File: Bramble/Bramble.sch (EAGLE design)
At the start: 29 parts

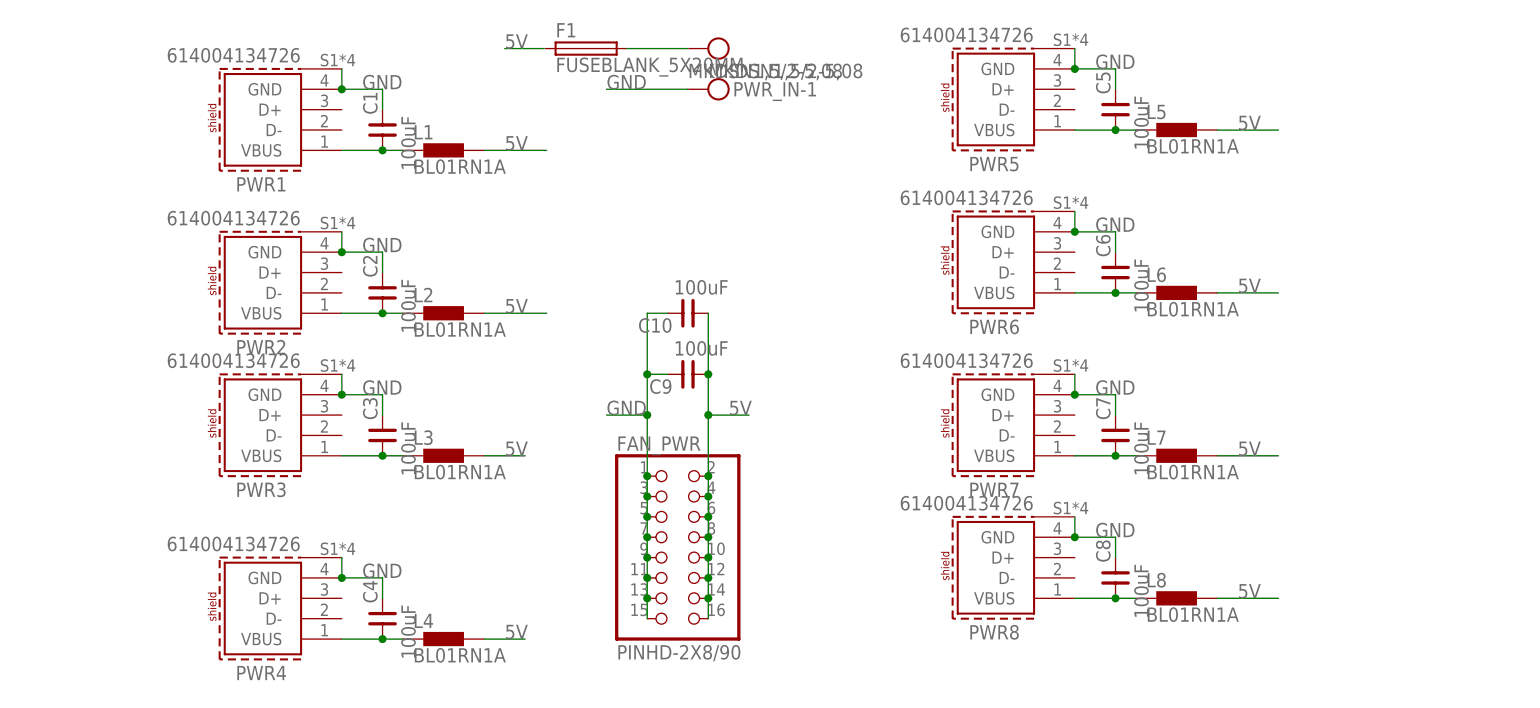
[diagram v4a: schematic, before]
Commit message: Reduction to 4 ports and SMD parts
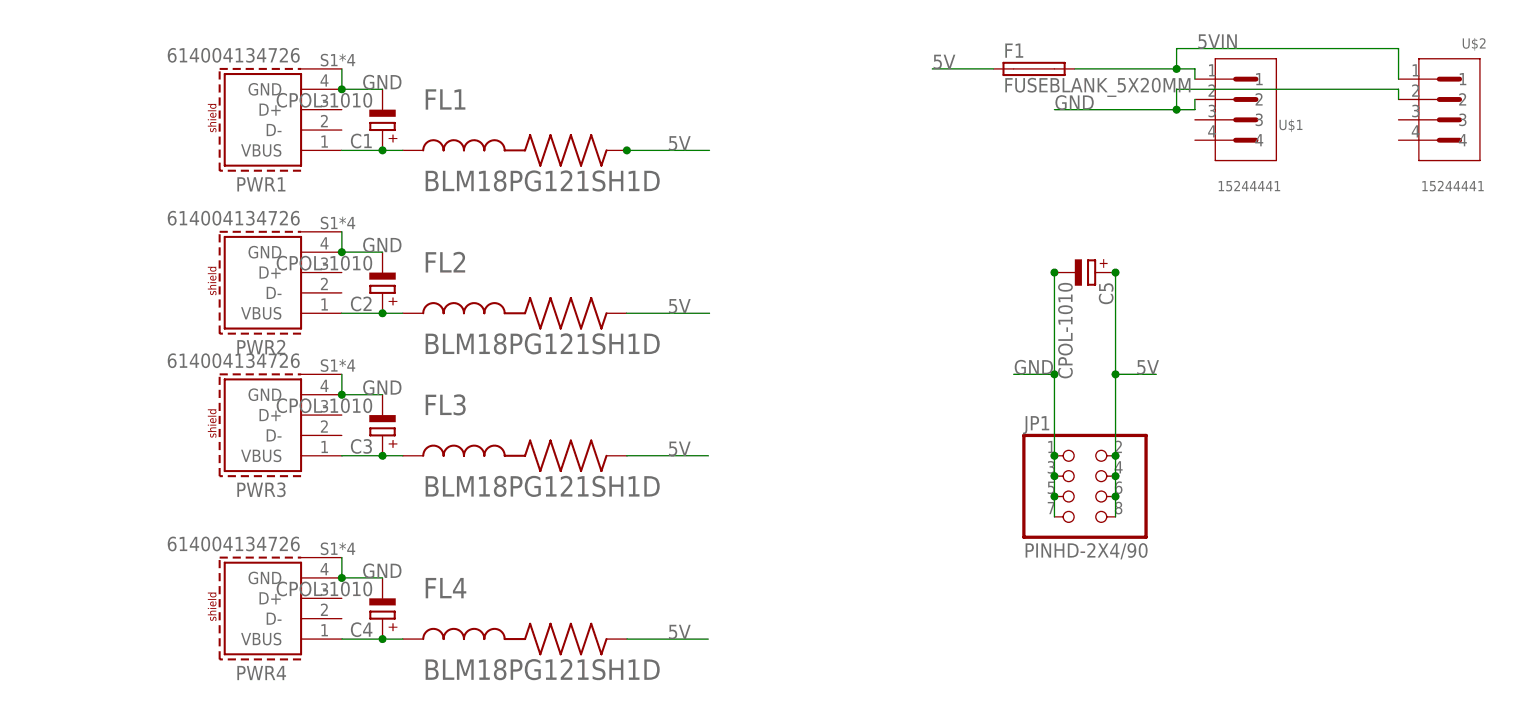
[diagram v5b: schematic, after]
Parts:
- removed C10, C6, C7, C8, C9: 100uF, cap-master:CBP-ENP-020-050
- removed FAN_PWR: PINHD-2X8/90, Connector:PINHD-2X8/90
- removed L1, L2, L3, L4, L5, L6, L7, L8: BL01RN1A, inductors:BL01RN1A
- removed PWR5, PWR6, PWR7, PWR8: 614004134726, Wurth_Connectors_WR-USB:614004134726
- removed PWR_IN: MKDSN1,5/2-5,08, con-phoenix-508:MKDSN1,5/2-5,08
- added FL1, FL2, FL3, FL4: BLM18PG121SH1D, BLM18PG121SH1D:BLM18PG121SH1D
- added JP1: PINHD-2X4/90, Connector:PINHD-2X4/90
- added U$1, U$2: 15244441, 15244441:15244441
- C1, C2, C3, C4, C5: value 100uF -> CPOL-1010; device cap-master:CBP-ENP-020-050 -> cap-vishay-153clv:CPOL-1010
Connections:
- removed net N$5: C5.1, L5.1, PWR5.VBUS
- removed net N$6: C6.1, L6.1, PWR6.VBUS
- removed net N$7: C7.1, L7.1, PWR7.VBUS
- removed net N$8: C8.1, L8.1, PWR8.VBUS
- removed net N$9: F1.2, PWR_IN-2.KL
- new net 5VIN: F1.2, U$1.1, U$2.1
- net 5V: now also C5.+, F1.1, FL1.2, FL2.2, FL3.2, FL4.2, JP1.2, JP1.4, JP1.6, JP1.8; no longer C10.1, C9.1, FAN_PWR.10, FAN_PWR.12, FAN_PWR.14, FAN_PWR.16, FAN_PWR.2, FAN_PWR.4, FAN_PWR.6, FAN_PWR.8, L1.2, L2.2, L3.2, L4.2, L5.2, L6.2, L7.2, L8.2
- net GND: now also C1.-, C2.-, C3.-, C4.-, C5.-, JP1.1, JP1.3, JP1.5, JP1.7, U$1.2, U$2.2; no longer C1.2, C10.2, C2.2, C3.2, C4.2, C5.2, C6.2, C7.2, C8.2, C9.2, FAN_PWR.1, FAN_PWR.11, FAN_PWR.13, FAN_PWR.15, FAN_PWR.3, FAN_PWR.5, FAN_PWR.7, FAN_PWR.9, PWR5.GND, PWR5.SHIELD, PWR6.GND, PWR6.SHIELD, PWR7.GND, PWR7.SHIELD, PWR8.GND, PWR8.SHIELD, PWR_IN-1.KL
- net N$1: now also C1.+, FL1.1; no longer C1.1, L1.1
- net N$2: now also C2.+, FL2.1; no longer C2.1, L2.1
- net N$3: now also C4.+, FL4.1; no longer C4.1, L4.1
- net N$4: now also C3.+, FL3.1; no longer C3.1, L3.1
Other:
- moved on the sheet: F1

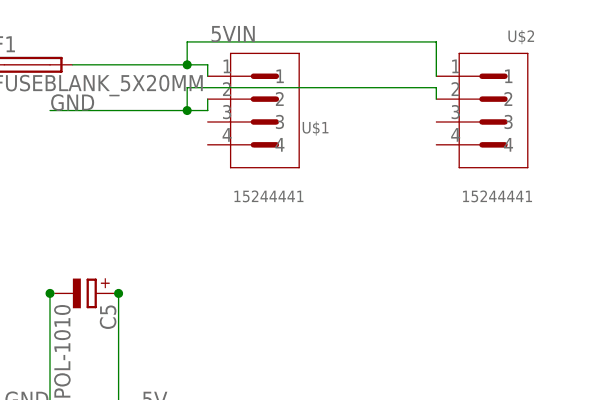
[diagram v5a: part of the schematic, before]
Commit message: Tweaked labels
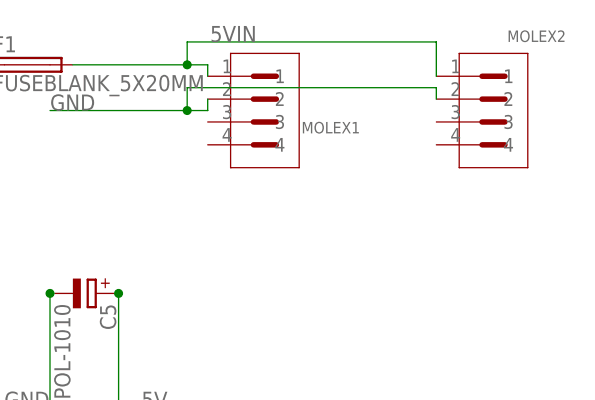
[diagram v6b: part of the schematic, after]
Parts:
- renumbered U$1 to MOLEX1, U$2 to MOLEX2
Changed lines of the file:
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@@
 <part name="FL3" library="BLM18PG121SH1D" deviceset="BLM18PG121SH1D" device=""/>
 <part name="FL4" library="BLM18PG121SH1D" deviceset="BLM18PG121SH1D" device=""/>
-<part name="U$1" library="15244441" deviceset="15244441" device=""/>
-<part name="U$2" library="15244441" deviceset="15244441" device=""/>
+<part name="MOLEX1" library="15244441" deviceset="15244441" device=""/>
+<part name="MOLEX2" library="15244441" deviceset="15244441" device=""/>
 </parts>
 <sheets>
@@
 <attribute name="VALUE" x="12.69" y="-2.546640625" size="2.54331875" layer="96"/>
 </instance>
-<instance part="U$1" gate="G$1" x="116.84" y="68.58" smashed="yes">
+<instance part="MOLEX1" gate="G$1" x="116.84" y="68.58" smashed="yes">
 <attribute name="NAME" x="119.37916875" y="66.041240625" size="1.270209375" layer="95"/>
-<attribute name="VALUE" x="111.75308125" y="58.4062" size="1.27173125" layer="96"/>
-</instance>
-<instance part="U$2" gate="G$1" x="142.24" y="68.58" smashed="yes">
+</instance>
+<instance part="MOLEX2" gate="G$1" x="142.24" y="68.58" smashed="yes">
 <attribute name="NAME" x="142.23916875" y="76.201240625" size="1.270209375" layer="95"/>
-<attribute name="VALUE" x="137.15308125" y="58.4062" size="1.27173125" layer="96"/>
 </instance>
 </instances>
@@
 <label x="91.44" y="68.58" size="1.778" layer="95"/>
 <wire x1="91.44" y1="68.58" x2="106.68" y2="68.58" width="0.1524" layer="91"/>
-<pinref part="U$1" gate="G$1" pin="2"/>
+<pinref part="MOLEX1" gate="G$1" pin="2"/>
 <wire x1="106.68" y1="68.58" x2="108.966" y2="68.58" width="0.1524" layer="91"/>
 <wire x1="108.966" y1="69.85" x2="108.966" y2="68.58" width="0.1524" layer="91"/>
-<pinref part="U$2" gate="G$1" pin="2"/>
+<pinref part="MOLEX2" gate="G$1" pin="2"/>
 <wire x1="134.366" y1="69.85" x2="134.366" y2="71.12" width="0.1524" layer="91"/>
 <wire x1="134.366" y1="71.12" x2="106.68" y2="71.12" width="0.1524" layer="91"/>
@@
 <pinref part="F1" gate="G$1" pin="2"/>
 <wire x1="93.98" y1="73.66" x2="106.68" y2="73.66" width="0.1524" layer="91"/>
-<pinref part="U$1" gate="G$1" pin="1"/>
+<pinref part="MOLEX1" gate="G$1" pin="1"/>
 <wire x1="106.68" y1="73.66" x2="108.966" y2="73.66" width="0.1524" layer="91"/>
 <wire x1="108.966" y1="72.39" x2="108.966" y2="73.66" width="0.1524" layer="91"/>
-<pinref part="U$2" gate="G$1" pin="1"/>
+<pinref part="MOLEX2" gate="G$1" pin="1"/>
 <wire x1="134.366" y1="72.39" x2="134.366" y2="76.2" width="0.1524" layer="91"/>
 <wire x1="134.366" y1="76.2" x2="106.68" y2="76.2" width="0.1524" layer="91"/>

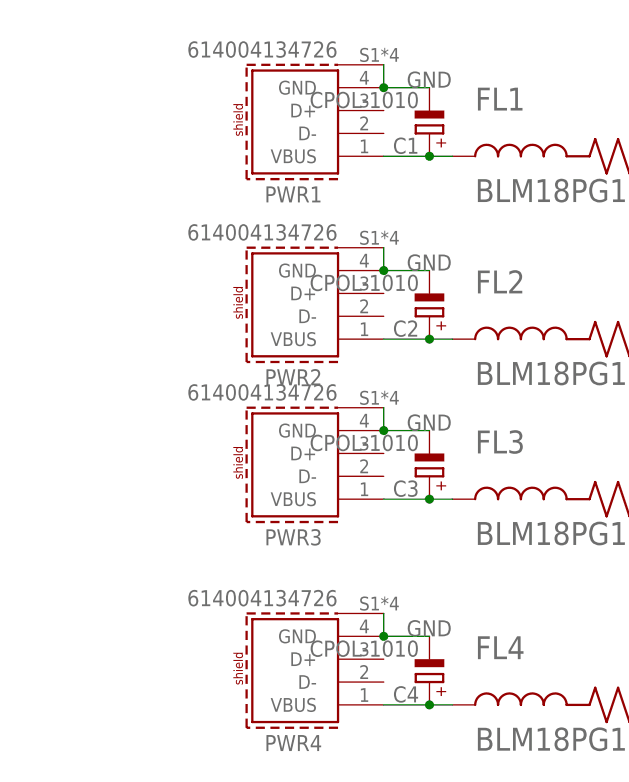
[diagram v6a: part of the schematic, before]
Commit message: 2x 2 port usb
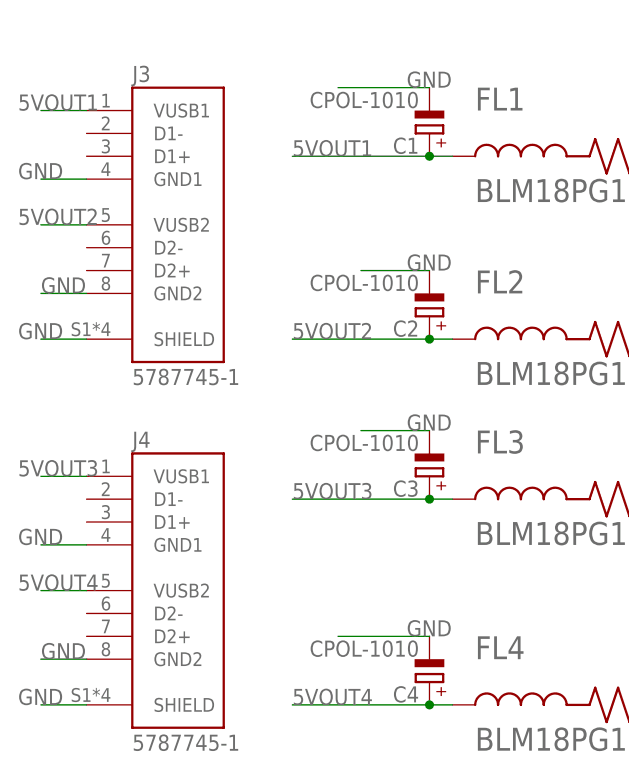
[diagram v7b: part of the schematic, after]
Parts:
- removed PWR1, PWR2, PWR3, PWR4: 614004134726, Wurth_Connectors_WR-USB:614004134726
- added J3, J4: 5787745-1, 5787745-1:5787745-1
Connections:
- removed net N$1: C1.+, FL1.1, PWR1.VBUS
- removed net N$2: C2.+, FL2.1, PWR2.VBUS
- removed net N$3: C4.+, FL4.1, PWR4.VBUS
- removed net N$4: C3.+, FL3.1, PWR3.VBUS
- new net 5VOUT1: C1.+, FL1.1, J3.VUSB1
- new net 5VOUT2: C2.+, FL2.1, J3.VUSB2
- new net 5VOUT3: C3.+, FL3.1, J4.VUSB1
- new net 5VOUT4: C4.+, FL4.1, J4.VUSB2
- net GND: now also J3.GND1, J3.GND2, J3.SHIELD, J4.GND1, J4.GND2, J4.SHIELD; no longer PWR1.GND, PWR1.SHIELD, PWR2.GND, PWR2.SHIELD, PWR3.GND, PWR3.SHIELD, PWR4.GND, PWR4.SHIELD

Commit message: joined 1 and 2  aaand 3 and 4
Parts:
- FL1, FL2, FL3, FL4: value BLM18PG121SH1D -> BLM18KG121TN1D
- renumbered J3 to USB12, J4 to USB34
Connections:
- removed net 5VOUT1: C1.+, FL1.1, USB12.VUSB1
- removed net 5VOUT2: C2.+, FL2.1, USB12.VUSB2
- removed net 5VOUT3: C3.+, FL3.1, USB34.VUSB1
- removed net 5VOUT4: C4.+, FL4.1, USB34.VUSB2
- new net 5VOUT12: C1.+, C2.+, FL1.1, FL2.1, USB12.VUSB1, USB12.VUSB2
- new net 5VOUT34: C3.+, C4.+, FL3.1, FL4.1, USB34.VUSB1, USB34.VUSB2
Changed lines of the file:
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@@
 <part name="C4" library="cap-vishay-153clv" deviceset="CPOL-1010" device=""/>
 <part name="C5" library="cap-vishay-153clv" deviceset="CPOL-1010" device=""/>
-<part name="FL1" library="BLM18PG121SH1D" deviceset="BLM18PG121SH1D" device=""/>
-<part name="FL2" library="BLM18PG121SH1D" deviceset="BLM18PG121SH1D" device=""/>
-<part name="FL3" library="BLM18PG121SH1D" deviceset="BLM18PG121SH1D" device=""/>
-<part name="FL4" library="BLM18PG121SH1D" deviceset="BLM18PG121SH1D" device=""/>
+<part name="FL1" library="BLM18PG121SH1D" deviceset="BLM18PG121SH1D" device="" value="BLM18KG121TN1D"/>
+<part name="FL2" library="BLM18PG121SH1D" deviceset="BLM18PG121SH1D" device="" value="BLM18KG121TN1D"/>
+<part name="FL3" library="BLM18PG121SH1D" deviceset="BLM18PG121SH1D" device="" value="BLM18KG121TN1D"/>
+<part name="FL4" library="BLM18PG121SH1D" deviceset="BLM18PG121SH1D" device="" value="BLM18KG121TN1D"/>
 <part name="MOLEX1" library="15244441" deviceset="15244441" device=""/>
 <part name="MOLEX2" library="15244441" deviceset="15244441" device=""/>
-<part name="J3" library="5787745-1" deviceset="5787745-1" device=""/>
-<part name="J4" library="5787745-1" deviceset="5787745-1" device=""/>
+<part name="USB12" library="5787745-1" deviceset="5787745-1" device=""/>
+<part name="USB34" library="5787745-1" deviceset="5787745-1" device=""/>
 </parts>
 <sheets>
@@
 <attribute name="NAME" x="142.23916875" y="76.201240625" size="1.270209375" layer="95"/>
 </instance>
-<instance part="J3" gate="G$1" x="-20.32" y="55.88" smashed="yes">
+<instance part="USB12" gate="G$1" x="-20.32" y="55.88" smashed="yes">
 <attribute name="NAME" x="-25.400109375" y="71.7553" size="1.778040625" layer="95"/>
 <attribute name="VALUE" x="-25.40351875" y="38.0877" size="1.77923125" layer="96"/>
 </instance>
-<instance part="J4" gate="G$1" x="-20.32" y="15.24" smashed="yes">
+<instance part="USB34" gate="G$1" x="-20.32" y="15.24" smashed="yes">
 <attribute name="NAME" x="-25.400109375" y="31.1153" size="1.778040625" layer="95"/>
 <attribute name="VALUE" x="-25.40351875" y="-2.5523" size="1.77923125" layer="96"/>
@@
 <segment>
 <wire x1="-35.56" y1="43.18" x2="-30.48" y2="43.18" width="0.1524" layer="91"/>
-<pinref part="J3" gate="G$1" pin="SHIELD"/>
+<pinref part="USB12" gate="G$1" pin="SHIELD"/>
 <label x="-38.1" y="43.18" size="1.778" layer="95"/>
 </segment>
 <segment>
 <wire x1="-35.56" y1="2.54" x2="-30.48" y2="2.54" width="0.1524" layer="91"/>
-<pinref part="J4" gate="G$1" pin="SHIELD"/>
+<pinref part="USB34" gate="G$1" pin="SHIELD"/>
 <label x="-38.1" y="2.54" size="1.778" layer="95"/>
 </segment>
 <segment>
 <wire x1="-35.56" y1="20.32" x2="-30.48" y2="20.32" width="0.1524" layer="91"/>
-<pinref part="J4" gate="G$1" pin="GND1"/>
+<pinref part="USB34" gate="G$1" pin="GND1"/>
 <label x="-38.1" y="20.32" size="1.778" layer="95"/>
 </segment>
 <segment>
 <wire x1="-35.56" y1="48.26" x2="-30.48" y2="48.26" width="0.1524" layer="91"/>
-<pinref part="J3" gate="G$1" pin="GND2"/>
+<pinref part="USB12" gate="G$1" pin="GND2"/>
 <label x="-35.56" y="48.26" size="1.778" layer="95"/>
 </segment>
 <segment>
 <wire x1="-35.56" y1="60.96" x2="-30.48" y2="60.96" width="0.1524" layer="91"/>
-<pinref part="J3" gate="G$1" pin="GND1"/>
+<pinref part="USB12" gate="G$1" pin="GND1"/>
 <label x="-38.1" y="60.96" size="1.778" layer="95"/>
 </segment>
 <segment>
 <wire x1="-35.56" y1="7.62" x2="-30.48" y2="7.62" width="0.1524" layer="91"/>
-<pinref part="J4" gate="G$1" pin="GND2"/>
+<pinref part="USB34" gate="G$1" pin="GND2"/>
 <label x="-35.56" y="7.62" size="1.778" layer="95"/>
 </segment>
@@
 </segment>
 </net>
-<net name="5VOUT1" class="0">
+<net name="5VOUT12" class="0">
 <segment>
 <wire x1="-35.56" y1="68.58" x2="-30.48" y2="68.58" width="0.1524" layer="91"/>
-<pinref part="J3" gate="G$1" pin="VUSB1"/>
+<pinref part="USB12" gate="G$1" pin="VUSB1"/>
 <label x="-38.1" y="68.58" size="1.778" layer="95"/>
+</segment>
+<segment>
+<wire x1="-35.56" y1="55.88" x2="-30.48" y2="55.88" width="0.1524" layer="91"/>
+<pinref part="USB12" gate="G$1" pin="VUSB2"/>
+<label x="-38.1" y="55.88" size="1.778" layer="95"/>
 </segment>
 <segment>
@@
 <label x="-7.62" y="63.5" size="1.778" layer="95"/>
 </segment>
-</net>
-<net name="5VOUT2" class="0">
-<segment>
-<wire x1="-35.56" y1="55.88" x2="-30.48" y2="55.88" width="0.1524" layer="91"/>
-<pinref part="J3" gate="G$1" pin="VUSB2"/>
-<label x="-38.1" y="55.88" size="1.778" layer="95"/>
-</segment>
 <segment>
 <wire x1="-7.62" y1="43.18" x2="7.62" y2="43.18" width="0.1524" layer="91"/>
@@
 </segment>
 </net>
-<net name="5VOUT3" class="0">
+<net name="5VOUT34" class="0">
 <segment>
 <wire x1="-35.56" y1="27.94" x2="-30.48" y2="27.94" width="0.1524" layer="91"/>
-<pinref part="J4" gate="G$1" pin="VUSB1"/>
+<pinref part="USB34" gate="G$1" pin="VUSB1"/>
 <label x="-38.1" y="27.94" size="1.778" layer="95"/>
 </segment>
@@
 <label x="-7.62" y="25.4" size="1.778" layer="95"/>
 </segment>
-</net>
-<net name="5VOUT4" class="0">
 <segment>
 <wire x1="-35.56" y1="15.24" x2="-30.48" y2="15.24" width="0.1524" layer="91"/>
-<pinref part="J4" gate="G$1" pin="VUSB2"/>
+<pinref part="USB34" gate="G$1" pin="VUSB2"/>
 <label x="-38.1" y="15.24" size="1.778" layer="95"/>
 </segment>
